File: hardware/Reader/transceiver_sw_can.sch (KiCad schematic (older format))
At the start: 12 parts

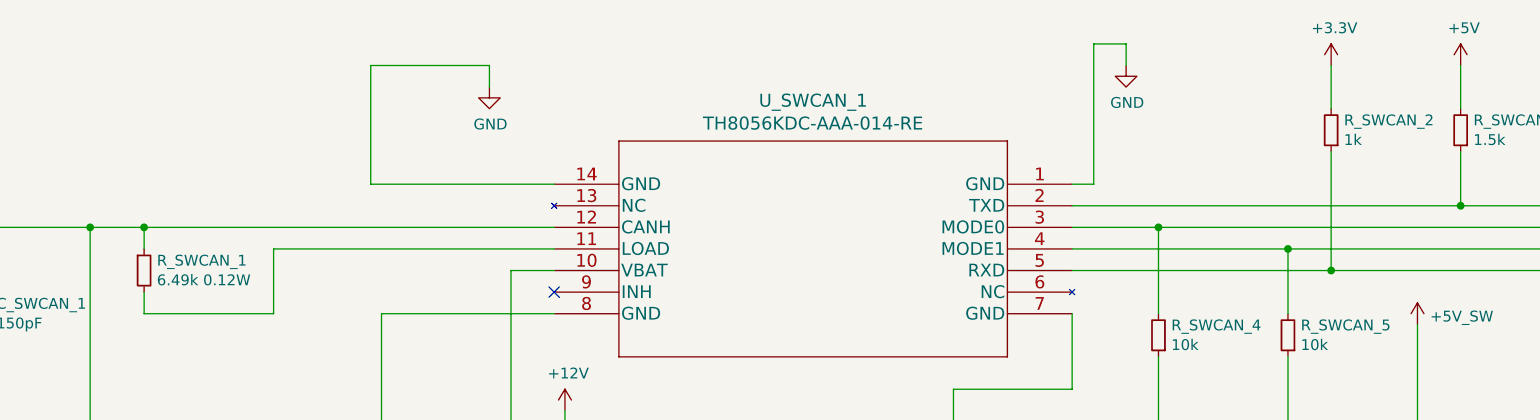
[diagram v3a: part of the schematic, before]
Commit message: Fixed bugs on the reader schematic. Exported Schematic Electrical report
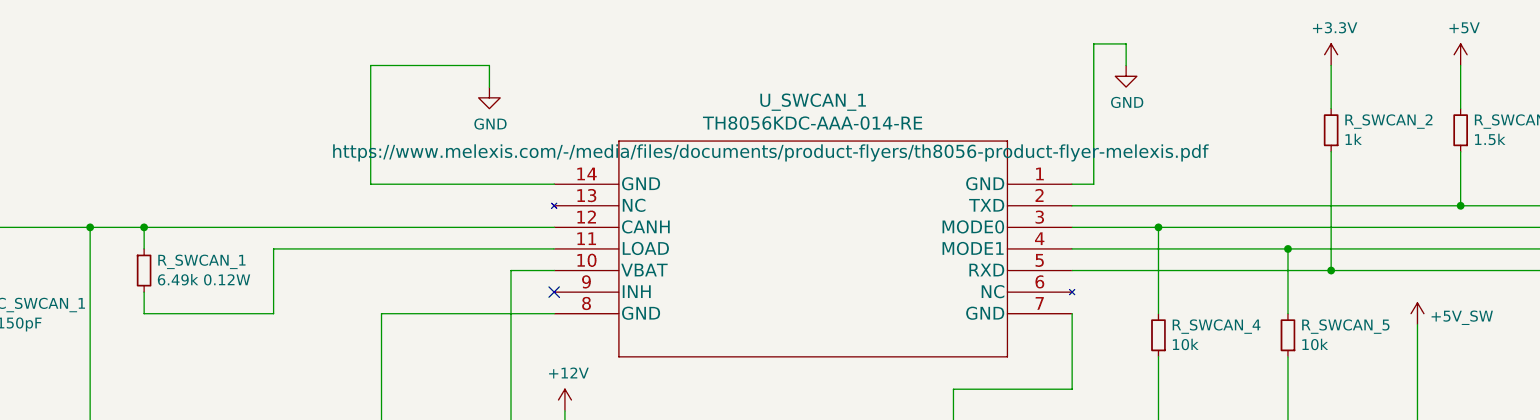
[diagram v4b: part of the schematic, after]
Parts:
- C_SWCAN_1: Manufacturer (none) -> Yageo; Part Name (none) -> CC0402JRNPO8BN151; Vendor (none) -> DigiKey Canada; digikeypn (none) -> 311-3747-1-ND
- C_SWCAN_2: Manufacturer (none) -> Kermet; Vendor (none) -> DigiKey Canada; digikeypn (none) -> 399-7029-1-ND
- J_SWCAN_1: Manufacturer (none) -> TE Connectivity AMP Connectors; Vendor (none) -> DigiKey Canada; digikeypn (none) -> A113314-ND
- Q_SWCAN_1: Manufacturer (none) -> Nexperia USA Inc.; Part Name (none) -> NX7002AK,215; Vendor (none) -> DigiKey Canada; digikeypn (none) -> 1727-1289-1-ND
- R_SWCAN_1: Manufacturer (none) -> Yageo; Vendor (none) -> DigiKey Canada; digikeypn (none) -> 311-6.49KCRCT-ND
- R_SWCAN_2: Manufacturer (none) -> Samsung Electro-Mechanics; Vendor (none) -> DigiKey Canada; digikeypn (none) -> 1276-3484-1-ND
- R_SWCAN_3: Manufacturer (none) -> Yageo; Vendor (none) -> DigiKey Canada; digikeypn (none) -> 311-1.50KHRCT-ND
- R_SWCAN_4, R_SWCAN_5, R_SWCAN_7: Manufacturer (none) -> Yageo; Vendor (none) -> DigiKey Canada; digikeypn (none) -> YAG2321CT-ND
- R_SWCAN_6: Manufacturer (none) -> Yageo; Vendor (none) -> DigiKey Canada; digikeypn (none) -> YAG2394CT-ND
- U_SWCAN_1: Manufacturer (none) -> Melexis Technologies NV; Part Name (none) -> TH8056KDC-AAA-014-RE; Vendor (none) -> DigiKey Canada; digikeypn (none) -> TH8056KDC-AAA-014-RECT-ND
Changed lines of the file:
@@
 F 1 "TH8056KDC-AAA-014-RE" H 8350 2731 60  0000 C CNN
 F 2 "footprints:TH8056KDC-AAA-014-RE" H 8350 2690 60  0001 C CNN
-F 3 "" H 7150 2450 60  0000 C CNN
+F 3 "https://www.melexis.com/-/media/files/documents/product-flyers/th8056-product-flyer-melexis.pdf" H 8550 2600 60  0000 C CNN
+F 4 "TH8056KDC-AAA-014-RE" H 7150 2450 50  0001 C CNN "Part Name"
+F 5 "Melexis Technologies NV" H 7150 2450 50  0001 C CNN "Manufacturer"
+F 6 "DigiKey Canada" H 7150 2450 50  0001 C CNN "Vendor"
+F 7 "TH8056KDC-AAA-014-RECT-ND" H 7150 2450 50  0001 C CNN "digikeypn"
 	1    7150 2450
 	-1   0    0    -1
@@
 F 3 "https://www.yageo.com/upload/media/product/productsearch/datasheet/rchip/PYu-RC_Group_51_RoHS_L_11.pdf" H 2600 4550 50  0001 C CNN
 F 4 "RC0201FR-07130RL" H 2600 4550 50  0001 C CNN "Part Name"
+F 5 "Yageo" H 2600 4550 50  0001 C CNN "Manufacturer"
+F 6 "DigiKey Canada" H 2600 4550 50  0001 C CNN "Vendor"
+F 7 "YAG2394CT-ND" H 2600 4550 50  0001 C CNN "digikeypn"
 	1    2600 4550
 	1    0    0    -1
@@
 F 5 "7" H 2500 5050 50  0001 L BNN "Field5"
 F 6 "IPC-7351B" H 2500 5050 50  0001 L BNN "Field6"
+F 7 "NX7002AK,215" H 2500 5050 50  0001 C CNN "Part Name"
+F 8 "Nexperia USA Inc." H 2500 5050 50  0001 C CNN "Manufacturer"
+F 9 "DigiKey Canada" H 2500 5050 50  0001 C CNN "Vendor"
+F 10 "1727-1289-1-ND" H 2500 5050 50  0001 C CNN "digikeypn"
 	1    2500 5050
 	1    0    0    -1
@@
 F 3 "https://www.yageo.com/upload/media/product/productsearch/datasheet/rchip/PYu-RT_1-to-0.01_RoHS_L_12.pdf" H 1950 5400 50  0001 C CNN
 F 4 "RT0603FRE0710KL" H 1950 5400 50  0001 C CNN "Part Name"
+F 5 "Yageo" H 1950 5400 50  0001 C CNN "Manufacturer"
+F 6 "DigiKey Canada" H 1950 5400 50  0001 C CNN "Vendor"
+F 7 "YAG2321CT-ND" H 1950 5400 50  0001 C CNN "digikeypn"
 	1    1950 5400
 	1    0    0    -1
@@
 F 3 "https://www.yageo.com/upload/media/product/productsearch/datasheet/rchip/PYu-RT_1-to-0.01_RoHS_L_12.pdf" H 2850 2850 50  0001 C CNN
 F 4 "RC0805FR-076K49L" H 2850 2850 50  0001 C CNN "Part Name"
+F 5 "Yageo" H 2850 2850 50  0001 C CNN "Manufacturer"
+F 6 "DigiKey Canada" H 2850 2850 50  0001 C CNN "Vendor"
+F 7 "311-6.49KCRCT-ND" H 2850 2850 50  0001 C CNN "digikeypn"
 	1    2850 2850
 	1    0    0    -1
@@
 F 3 "https://api.kemet.com/component-edge/download/specsheet/C1206C475K3RACAUTO.pdf" H 4300 3900 50  0001 C CNN
 F 4 "C1206C475K3RACAUTO" H 4300 3900 50  0001 C CNN "Part Name"
+F 5 "Kermet" H 4300 3900 50  0001 C CNN "Manufacturer"
+F 6 "DigiKey Canada" H 4300 3900 50  0001 C CNN "Vendor"
+F 7 "399-7029-1-ND" H 4300 3900 50  0001 C CNN "digikeypn"
 	1    4300 3900
 	0    1    1    0
@@
 F 3 "https://www.yageo.com/upload/media/product/productsearch/datasheet/rchip/PYu-RT_1-to-0.01_RoHS_L_12.pdf" H 7550 3150 50  0001 C CNN
 F 4 "RT0603FRE0710KL" H 7550 3150 50  0001 C CNN "Part Name"
+F 5 "Yageo" H 7550 3150 50  0001 C CNN "Manufacturer"
+F 6 "DigiKey Canada" H 7550 3150 50  0001 C CNN "Vendor"
+F 7 "YAG2321CT-ND" H 7550 3150 50  0001 C CNN "digikeypn"
 	1    7550 3150
 	-1   0    0    1
@@
 F 3 "https://media.digikey.com/pdf/Data%20Sheets/Samsung%20PDFs/RC_Series_ds.pdf" H 8350 2200 50  0001 C CNN
 F 4 "RC1608F102CS" H 8350 2200 50  0001 C CNN "Part Name"
+F 5 "Samsung Electro-Mechanics" H 8350 2200 50  0001 C CNN "Manufacturer"
+F 6 "DigiKey Canada" H 8350 2200 50  0001 C CNN "Vendor"
+F 7 "1276-3484-1-ND" H 8350 2200 50  0001 C CNN "digikeypn"
 	1    8350 2200
 	-1   0    0    1
@@
 F 3 "https://www.yageo.com/upload/media/product/productsearch/datasheet/rchip/PYu-RC_Group_51_RoHS_L_11.pdf" H 8950 2200 50  0001 C CNN
 F 4 "RC0603FR-071K5L" H 8950 2200 50  0001 C CNN "Part Name"
+F 5 "Yageo" H 8950 2200 50  0001 C CNN "Manufacturer"
+F 6 "DigiKey Canada" H 8950 2200 50  0001 C CNN "Vendor"
+F 7 "311-1.50KHRCT-ND" H 8950 2200 50  0001 C CNN "digikeypn"
 	1    8950 2200
 	-1   0    0    1
@@
 F 3 "https://www.yageo.com/upload/media/product/productsearch/datasheet/rchip/PYu-RT_1-to-0.01_RoHS_L_12.pdf" H 8150 3150 50  0001 C CNN
 F 4 "RT0603FRE0710KL" H 8150 3150 50  0001 C CNN "Part Name"
+F 5 "Yageo" H 8150 3150 50  0001 C CNN "Manufacturer"
+F 6 "DigiKey Canada" H 8150 3150 50  0001 C CNN "Vendor"
+F 7 "YAG2321CT-ND" H 8150 3150 50  0001 C CNN "digikeypn"
 	1    8150 3150
 	-1   0    0    1
@@
 F 3 "https://www.te.com/commerce/DocumentDelivery/DDEController?Action=srchrtrv&DocNm=282832&DocType=Customer+Drawing&DocLang=English" H 3128 3594 60  0001 L CNN
 F 4 "282832-2" H 2600 3750 50  0001 C CNN "Part Name"
+F 5 "DigiKey Canada" H 2600 3750 50  0001 C CNN "Vendor"
+F 6 "TE Connectivity AMP Connectors" H 2600 3750 50  0001 C CNN "Manufacturer"
+F 7 "A113314-ND" H 2600 3750 50  0001 C CNN "digikeypn"
 	1    2600 3750
 	1    0    0    -1
@@
 F 2 "footprints:CAPC1005X55N" H 2088 2900 50  0001 C CNN
 F 3 "https://www.yageo.com/upload/media/product/productsearch/datasheet/mlcc/UPY-GP_NP0_16V-to-50V_18.pdf" H 2050 3050 50  0001 C CNN
+F 4 "CC0402JRNPO8BN151" H 2050 3050 50  0001 C CNN "Part Name"
+F 5 "Yageo" H 2050 3050 50  0001 C CNN "Manufacturer"
+F 6 "DigiKey Canada" H 2050 3050 50  0001 C CNN "Vendor"
+F 7 "311-3747-1-ND" H 2050 3050 50  0001 C CNN "digikeypn"
 	1    2050 3050
 	1    0    0    -1

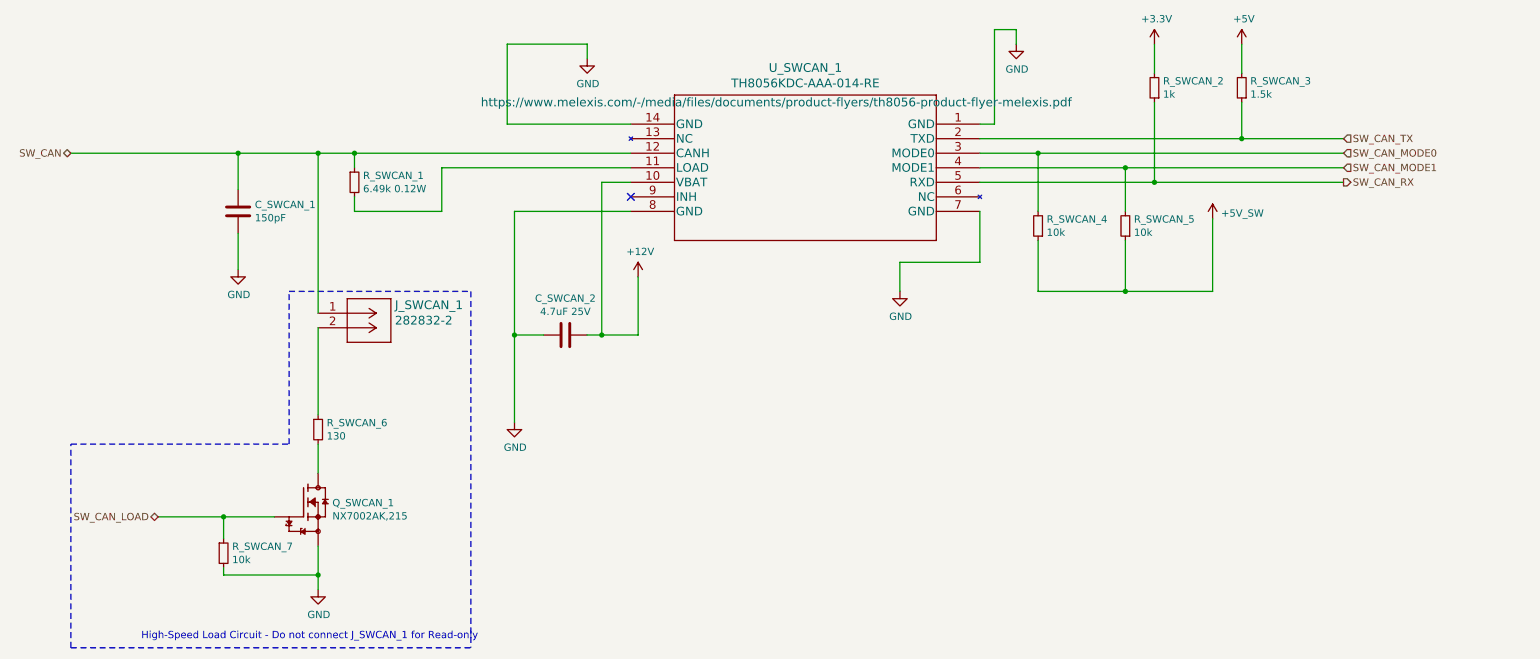
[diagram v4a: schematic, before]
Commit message: Fixed wiring issue on ESD Protection
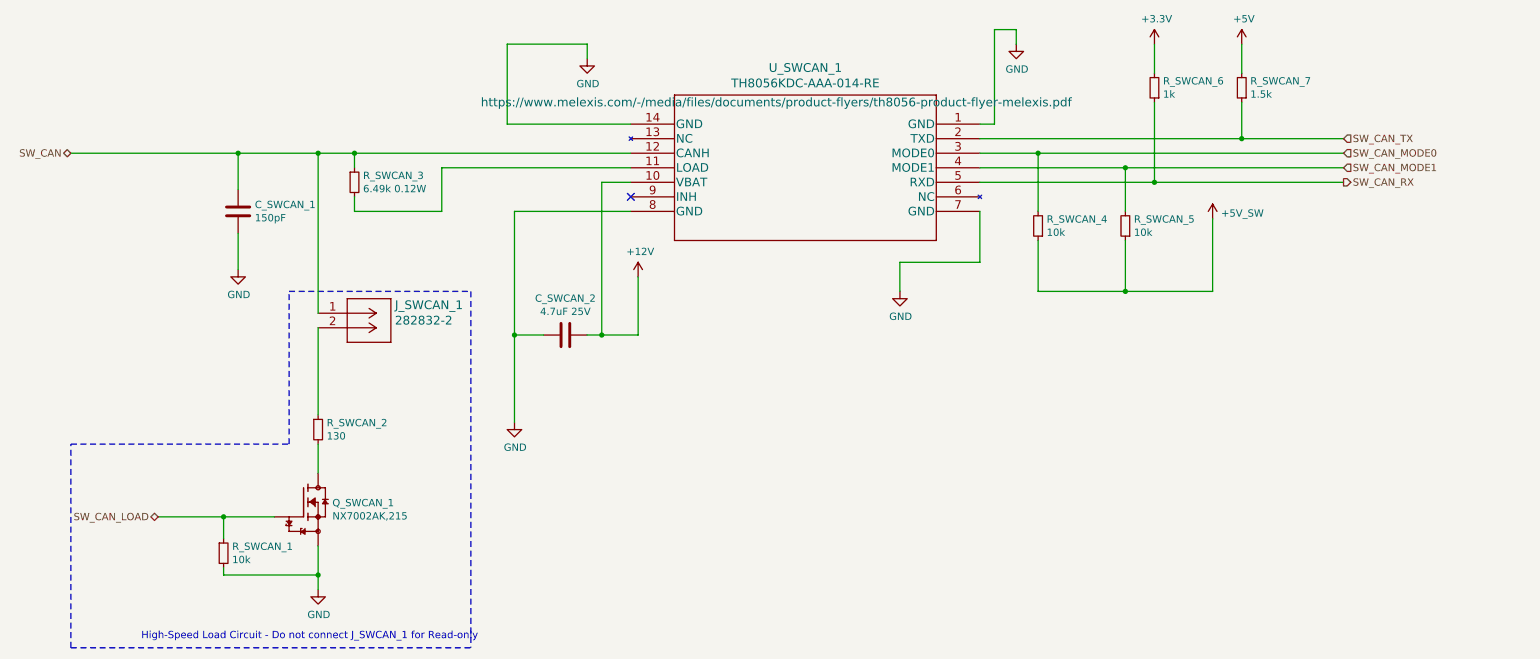
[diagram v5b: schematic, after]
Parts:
- renumbered R_SWCAN_7 to R_SWCAN_1, R_SWCAN_6 to R_SWCAN_2, R_SWCAN_1 to R_SWCAN_3, R_SWCAN_2 to R_SWCAN_6, R_SWCAN_3 to R_SWCAN_7
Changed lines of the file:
@@
 $EndComp
 $Comp
-L power:GND #PWR0182
+L power:GND #PWR046
 U 1 1 5FBCD97D
 P 2050 3450
-F 0 "#PWR0182" H 2050 3200 50  0001 C CNN
+F 0 "#PWR046" H 2050 3200 50  0001 C CNN
 F 1 "GND" H 2055 3277 50  0000 C CNN
 F 2 "" H 2050 3450 50  0001 C CNN
@@
 $EndComp
 $Comp
-L power:GND #PWR0183
+L power:GND #PWR048
 U 1 1 5FBCDB6B
 P 3950 4500
-F 0 "#PWR0183" H 3950 4250 50  0001 C CNN
+F 0 "#PWR048" H 3950 4250 50  0001 C CNN
 F 1 "GND" H 3955 4327 50  0000 C CNN
 F 2 "" H 3950 4500 50  0001 C CNN
@@
 $EndComp
 $Comp
-L Device:R_Small R_SWCAN_6
+L Device:R_Small R_SWCAN_2
 U 1 1 5FBCE6CE
 P 2600 4550
-F 0 "R_SWCAN_6" H 2659 4596 50  0000 L CNN
+F 0 "R_SWCAN_2" H 2659 4596 50  0000 L CNN
 F 1 "130" H 2659 4505 50  0000 L CNN
 F 2 "footprints:RESC0603X26N" H 2600 4550 50  0001 C CNN
@@
 $EndComp
 $Comp
-L Device:R_Small R_SWCAN_7
+L Device:R_Small R_SWCAN_1
 U 1 1 5FBCFFA6
 P 1950 5400
-F 0 "R_SWCAN_7" H 2009 5446 50  0000 L CNN
+F 0 "R_SWCAN_1" H 2009 5446 50  0000 L CNN
 F 1 "10k" H 2009 5355 50  0000 L CNN
 F 2 "footprints:RESC1608X55N" H 1950 5400 50  0001 C CNN
@@
 	2600 4850 2600 4650
 $Comp
-L power:GND #PWR0184
+L power:GND #PWR047
 U 1 1 5FBD183F
 P 2600 5650
-F 0 "#PWR0184" H 2600 5400 50  0001 C CNN
+F 0 "#PWR047" H 2600 5400 50  0001 C CNN
 F 1 "GND" H 2605 5477 50  0000 C CNN
 F 2 "" H 2600 5650 50  0001 C CNN
@@
 	2600 5550 2600 5650
 $Comp
-L Device:R_Small R_SWCAN_1
+L Device:R_Small R_SWCAN_3
 U 1 1 5FBD3FD7
 P 2850 2850
-F 0 "R_SWCAN_1" H 2909 2896 50  0000 L CNN
+F 0 "R_SWCAN_3" H 2909 2896 50  0000 L CNN
 F 1 "6.49k 0.12W" H 2909 2805 50  0000 L CNN
 F 2 "footprints:RESC1608X55N" H 2850 2850 50  0001 C CNN
@@
 NoConn ~ 4750 2950
 $Comp
-L power:GND #PWR0185
+L power:GND #PWR051
 U 1 1 5FBD540B
 P 6600 3600
-F 0 "#PWR0185" H 6600 3350 50  0001 C CNN
+F 0 "#PWR051" H 6600 3350 50  0001 C CNN
 F 1 "GND" H 6605 3427 50  0000 C CNN
 F 2 "" H 6600 3600 50  0001 C CNN
@@
 $EndComp
 $Comp
-L power:GND #PWR0186
+L power:GND #PWR049
 U 1 1 5FBD58BC
 P 4450 2000
-F 0 "#PWR0186" H 4450 1750 50  0001 C CNN
+F 0 "#PWR049" H 4450 1750 50  0001 C CNN
 F 1 "GND" H 4455 1827 50  0000 C CNN
 F 2 "" H 4450 2000 50  0001 C CNN
@@
 	4550 3900 4550 2850
 $Comp
-L power:+12V #PWR0187
+L power:+12V #PWR050
 U 1 1 5FBD853C
 P 4800 3500
-F 0 "#PWR0187" H 4800 3350 50  0001 C CNN
+F 0 "#PWR050" H 4800 3350 50  0001 C CNN
 F 1 "+12V" H 4815 3673 50  0000 C CNN
 F 2 "" H 4800 3500 50  0001 C CNN
@@
 	3950 3900 3950 4500
 $Comp
-L power:GND #PWR0188
+L power:GND #PWR052
 U 1 1 5FBDCE7D
 P 7400 1900
-F 0 "#PWR0188" H 7400 1650 50  0001 C CNN
+F 0 "#PWR052" H 7400 1650 50  0001 C CNN
 F 1 "GND" H 7405 1727 50  0000 C CNN
 F 2 "" H 7400 1900 50  0001 C CNN
@@
 	7150 2650 7550 2650
 $Comp
-L power:+5V #PWR0189
+L power:+5V #PWR055
 U 1 1 5FBE0112
 P 8950 1900
-F 0 "#PWR0189" H 8950 1750 50  0001 C CNN
+F 0 "#PWR055" H 8950 1750 50  0001 C CNN
 F 1 "+5V" H 8965 2073 50  0000 C CNN
 F 2 "" H 8950 1900 50  0001 C CNN
@@
 $EndComp
 $Comp
-L power:+3.3V #PWR0190
+L power:+3.3V #PWR053
 U 1 1 5FBE0764
 P 8350 1900
-F 0 "#PWR0190" H 8350 1750 50  0001 C CNN
+F 0 "#PWR053" H 8350 1750 50  0001 C CNN
 F 1 "+3.3V" H 8365 2073 50  0000 C CNN
 F 2 "" H 8350 1900 50  0001 C CNN
@@
 $EndComp
 $Comp
-L CANtech:+5V_SW #PWR0191
+L CANtech:+5V_SW #PWR054
 U 1 1 5FBE0C6A
 P 8750 3100
-F 0 "#PWR0191" H 8750 3350 50  0001 C CNN
+F 0 "#PWR054" H 8750 3350 50  0001 C CNN
 F 1 "+5V_SW" H 8808 3137 50  0000 L CNN
 F 2 "" H 8000 3900 50  0001 C CNN
@@
 $EndComp
 $Comp
-L Device:R_Small R_SWCAN_2
+L Device:R_Small R_SWCAN_6
 U 1 1 5FBE18B8
 P 8350 2200
-F 0 "R_SWCAN_2" H 8291 2154 50  0000 R CNN
+F 0 "R_SWCAN_6" H 8291 2154 50  0000 R CNN
 F 1 "1k" H 8291 2245 50  0000 R CNN
 F 2 "footprints:RC1608F102CS" H 8350 2200 50  0001 C CNN
@@
 	7150 2850 8350 2850
 $Comp
-L Device:R_Small R_SWCAN_3
+L Device:R_Small R_SWCAN_7
 U 1 1 5FBE16BD
 P 8950 2200
-F 0 "R_SWCAN_3" H 8891 2154 50  0000 R CNN
+F 0 "R_SWCAN_7" H 8891 2154 50  0000 R CNN
 F 1 "1.5k" H 8891 2245 50  0000 R CNN
 F 2 "footprints:RESC1607X60N" H 8950 2200 50  0001 C CNN
